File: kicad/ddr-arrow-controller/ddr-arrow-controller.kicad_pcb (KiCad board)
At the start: 2 copper layers, 172 x 172 mm, 117 parts, among them IC1 JanSquareLib_TS30013-M033QFNR, J10 OPTO, J11 ST_POW, J12 ST_CAN, J13 Step Sensor, J2 A0, J3 A1, J4 A2, J5 A3, J6 AVR-ISP-6, SW1 SW_Push, SW2 SW_DIP_x04, U1 TJA1051T, U2 MCP2515-xSO, U3 ATmega328PB-AU, U4 TLP290, U5 TLP290, Y1 16MHz, Y2 8MHz

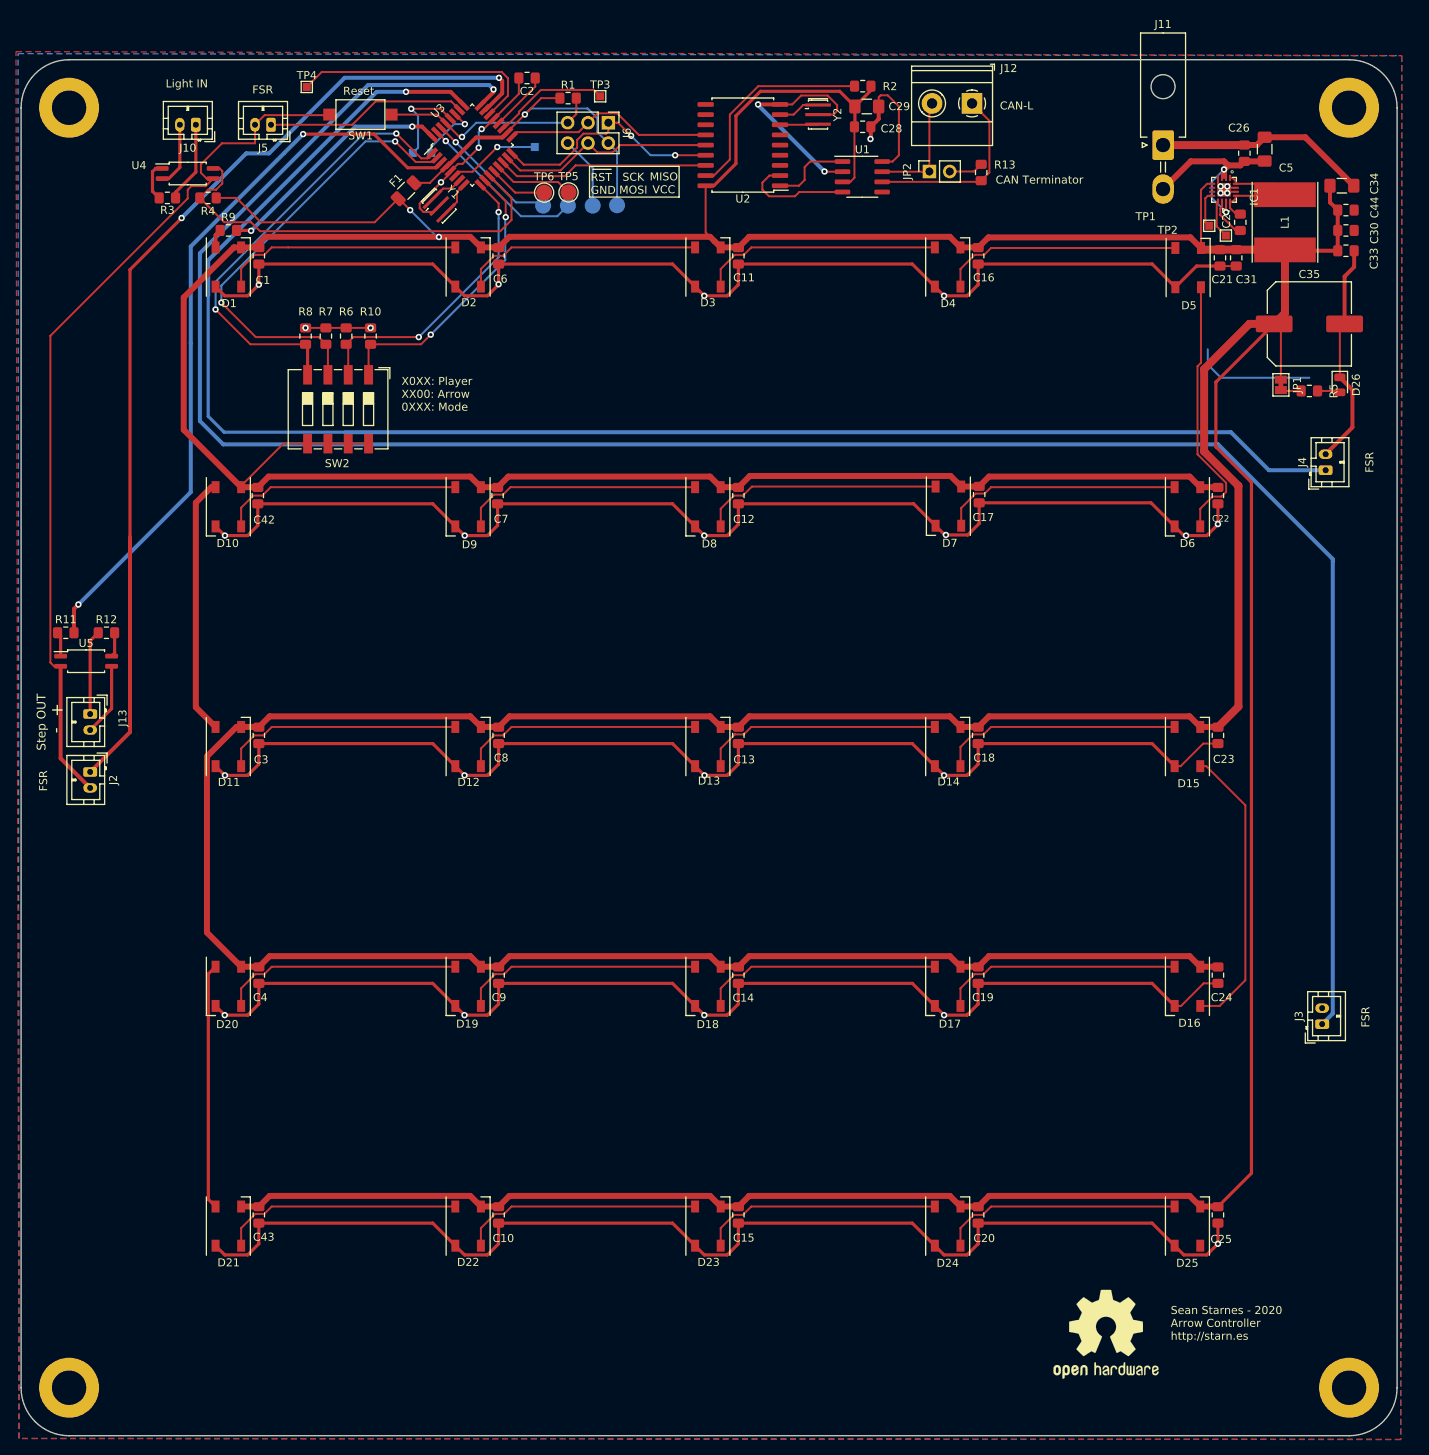
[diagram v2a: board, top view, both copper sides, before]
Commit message: Rerouted PCB
Fixed pcb plains. Fixed grounds. Fixed rounded pads. Exported Gerber files.
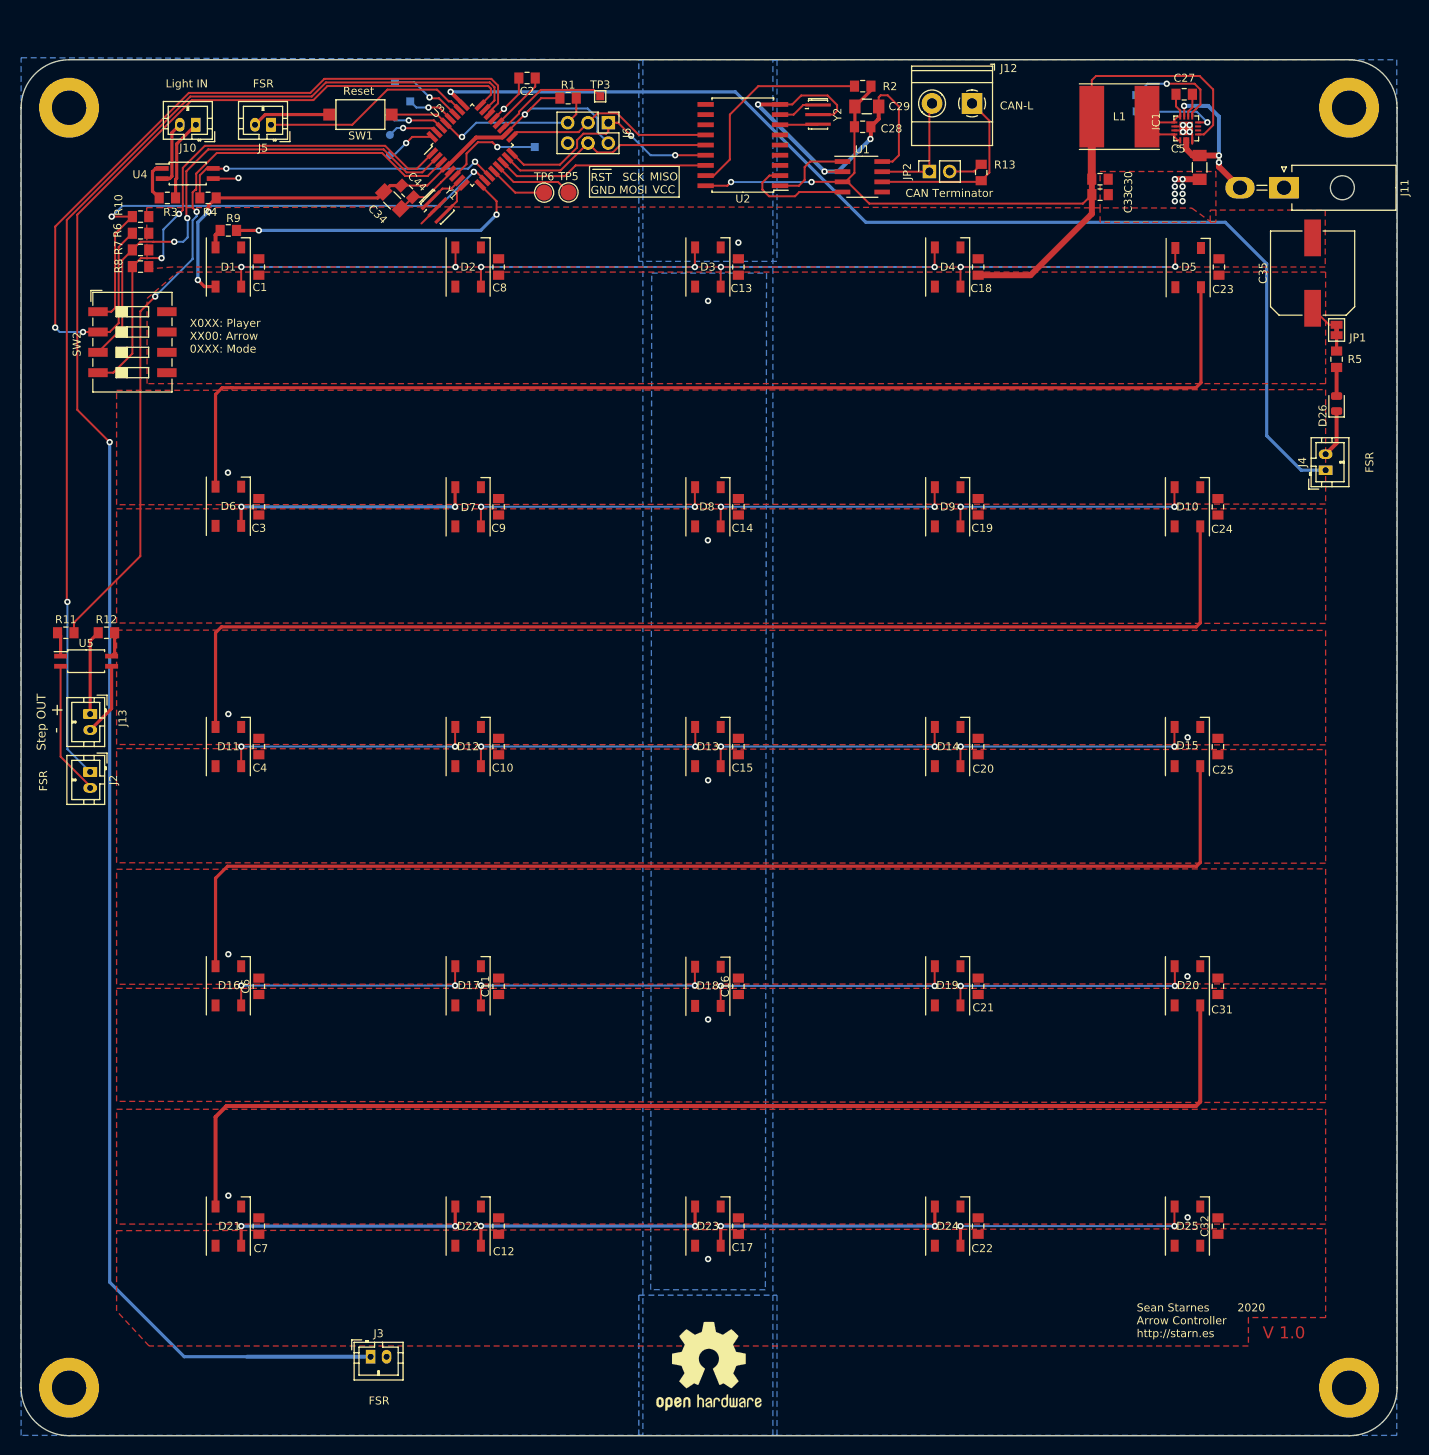
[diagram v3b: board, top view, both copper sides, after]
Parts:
- removed C26, C42, C43: 0.1uF, Capacitor_SMD:C_0805_2012Metric_Pad1.15x1.40mm_HandSolder
- removed F1: 1206L025YR, Fuse:Fuse_1206_3216Metric
- removed TP10: PC5, TestPoint:TestPoint_Pad_1.0x1.0mm
- removed TP11: 5V, TestPoint:TestPoint_Pad_D2.0mm
- removed TP12: GND, TestPoint:TestPoint_Pad_D2.0mm
- added C32: 0.1uF, Capacitor_SMD:C_0805_2012Metric_Pad1.15x1.40mm_HandSolder, F.Cu at (149.6, 145.8)
- added TP9: PD2, TestPoint:TestPoint_Pad_D1.0mm, B.Cu at (46.1, 11.9)
- C31: value 22uF -> 0.1uF
- TP1, TP2: moved to B.Cu
- TP13, TP14: footprint TestPoint:TestPoint_Pad_D2.0mm -> TestPoint:TestPoint_Pad_D1.0mm
- TP4: value PE3 -> PC4; moved to B.Cu
- TP8: value PC4 -> PC5
- moved J3 126.0 mm to (43.7, 162.1), turned to 0 degrees
- moved D16 119.9 mm to (25.9, 115.8), turned to 90 degrees
- moved D20 119.9 mm to (145.8, 115.8), turned to 90 degrees
- moved D6 119.9 mm to (25.9, 55.8), turned to 90 degrees
- moved D10 119.9 mm to (145.8, 55.9), turned to 90 degrees
- moved C34 118.7 mm to (46.4, 17.6), turned to 315 degrees
- moved C44 117.4 mm to (48.3, 16.5), turned to 315 degrees
- moved C17 96.3 mm to (89.7, 145.8), turned to 90 degrees
- moved C11 96.1 mm to (59.7, 115.8), turned to 90 degrees
- moved C16 96.1 mm to (89.7, 115.8), turned to 90 degrees
- moved C6 96.1 mm to (29.7, 115.8), turned to 90 degrees
- moved C12 96.1 mm to (59.7, 145.8), turned to 90 degrees
- moved C22 96.1 mm to (119.6, 145.8), turned to 90 degrees
- moved C7 96.1 mm to (29.7, 145.8), turned to 90 degrees
- moved C21 95.9 mm to (119.6, 115.8), turned to 90 degrees
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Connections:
- C1 pad 1: AVR_V -> +5V
- C10 pad 1: AVR_V -> +5V
- C11 pad 1: AVR_V -> +5V
- C12 pad 1: AVR_V -> +5V
- C13 pad 1: AVR_V -> +5V
- C14 pad 1: AVR_V -> +5V
- C15 pad 1: AVR_V -> +5V
- C16 pad 1: AVR_V -> +5V
- C17 pad 1: AVR_V -> +5V
- C18 pad 1: AVR_V -> +5V
- C19 pad 1: AVR_V -> +5V
- C20 pad 1: AVR_V -> +5V
- C21 pad 1: AVR_V -> +5V
- C22 pad 1: AVR_V -> +5V
- C23 pad 1: AVR_V -> +5V
- C24 pad 1: AVR_V -> +5V
- C25 pad 1: AVR_V -> +5V
- C28 pad 1: AVR_V -> +5V
- C29 pad 1: AVR_V -> +5V
- C3 pad 1: AVR_V -> +5V
- C30 pad 1: AVR_V -> +5V
- C31 pad 1: AVR_V -> +5V
- C33 pad 1: AVR_V -> +5V
- C34 pad 1: AVR_V -> +5V
- C35 pad 1: AVR_V -> +5V
- C4 pad 1: AVR_V -> +5V
- C44 pad 1: AVR_V -> +5V
- C6 pad 1: AVR_V -> +5V
- C7 pad 1: AVR_V -> +5V
- C8 pad 1: AVR_V -> +5V
- C9 pad 1: AVR_V -> +5V
- D1 pad 1: AVR_V -> GND
- D1 pad 3: GND -> +5V
- D10 pad 3: AVR_V -> +5V
- D11 pad 1: AVR_V -> GND
- D11 pad 3: GND -> +5V
- D12 pad 1: AVR_V -> GND
- D12 pad 3: GND -> +5V
- D13 pad 1: AVR_V -> GND
- D13 pad 3: GND -> +5V
- D14 pad 1: AVR_V -> GND
- D14 pad 3: GND -> +5V
- D15 pad 1: AVR_V -> GND
- D15 pad 3: GND -> +5V
- D16 pad 3: AVR_V -> +5V
- D17 pad 3: AVR_V -> +5V
- D18 pad 3: AVR_V -> +5V
- D19 pad 3: AVR_V -> +5V
- D2 pad 1: AVR_V -> GND
- D2 pad 3: GND -> +5V
- D20 pad 3: AVR_V -> +5V
- D21 pad 1: AVR_V -> GND
- D21 pad 3: GND -> +5V
- D22 pad 1: AVR_V -> GND
- D22 pad 3: GND -> +5V
- D23 pad 1: AVR_V -> GND
- D23 pad 3: GND -> +5V
- D24 pad 1: AVR_V -> GND
- D24 pad 3: GND -> +5V
- D25 pad 1: AVR_V -> GND
- D25 pad 3: GND -> +5V
- D3 pad 1: AVR_V -> GND
- D3 pad 3: GND -> +5V
- D4 pad 1: AVR_V -> GND
- D4 pad 3: GND -> +5V
- D5 pad 1: AVR_V -> GND
- D5 pad 3: GND -> +5V
- D6 pad 3: AVR_V -> +5V
- D7 pad 3: AVR_V -> +5V
- D8 pad 3: AVR_V -> +5V
- D9 pad 3: AVR_V -> +5V
- IC1 pad 5: AVR_V -> +5V
- J6 pad 2: AVR_V -> +5V
- JP1 pad 1: AVR_V -> +5V
- L1 pad 2: AVR_V -> +5V
- R1 pad 1: AVR_V -> +5V
- R2 pad 2: AVR_V -> +5V
- R4 pad 1: AVR_V -> +5V
- R6 pad 1: PD5 -> PE3
- R9 pad 2: PD2 -> PD5
- SW2 pad 2: PD5 -> PE3
- SW2 pad 5: AVR_V -> +5V
- SW2 pad 6: AVR_V -> +5V
- SW2 pad 7: AVR_V -> +5V
- SW2 pad 8: AVR_V -> +5V
- TP4 pad 1: PE3 -> PC4
- TP8 pad 1: PC4 -> PC5
- U1 pad 3: AVR_V -> +5V
- U2 pad 18: AVR_V -> +5V
- U3 pad 18: AVR_V -> +5V
- U3 pad 4: AVR_V -> +5V
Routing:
- net AVR_V: track 1074.3 -> 0.00 mm, vias 3 -> 0
- net GND: track 1010.5 -> 117.5 mm, vias 31 -> 25
- net +5V: track 0.00 -> 200.4 mm, vias 0 -> 10
- net Net-(D20-Pad4): track 30.7 -> 147.1 mm
- net Net-(D10-Pad4): track 32.3 -> 147.4 mm
- net Net-(D5-Pad4): track 33.6 -> 147.3 mm
- net Net-(D15-Pad4): track 36.5 -> 147.0 mm
- net PE3: track 31.7 -> 100.6 mm, vias 0 -> 2
- net PC2: track 203.4 -> 143.9 mm
- net PC1: track 276.7 -> 232.7 mm
- net PD6: track 36.2 -> 66.6 mm
- net PD2: track 30.4 -> 6.25 mm, vias 2 -> 1
- net PD1: track 21.3 -> 6.52 mm
- net PD7: track 54.3 -> 40.5 mm, vias 0 -> 2
- net PD3: track 56.8 -> 67.0 mm
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- added copper zone on B.Cu, net +5V
- added copper zone on F.Cu, net +5V
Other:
- board text added: "Sean Starnes 2020 Arrow Controller http://starn.es"
- board text added: "V 1.0"
- board text removed: "5V"
- board text removed: "Gnd"
- board text removed: "Sean Starnes - 2020 Arrow Controller http://starn.es"
